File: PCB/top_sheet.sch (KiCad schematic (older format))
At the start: 0 parts

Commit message: PCB Edge.Cuts Defined
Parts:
- added FID1, FID2, FID3: Fiducial, local:Fiducial_Front_Layer, symbol Fiducial
- added PN1: PCB_LABEL, symbol PCB_LABEL
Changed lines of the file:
@@
 $Descr A 11000 8500
 encoding utf-8
-Sheet 2 5
-Title ""
-Date ""
-Rev ""
-Comp ""
+Sheet 2 20
+Title "Christmas Tree Disco"
+Date "2017-08-01"
+Rev "01"
+Comp "www.GitHub.com/Cryochasm"
 Comment1 ""
 Comment2 ""
@@
 F1 "rgb_led_array.sch" 60
 $EndSheet
+$Comp
+L PCB_LABEL PN1
+U 1 1 59822887
+P 5000 2100
+F 0 "PN1" H 5528 2246 50  0000 L CNN
+F 1 "PCB_LABEL" H 5528 2155 50  0000 L CNN
+F 2 "" H 5150 1900 60  0001 C CNN
+F 3 "" H 5150 1900 60  0001 C CNN
+	1    5000 2100
+	1    0    0    -1
+$EndComp
+$Comp
+L Fiducial FID3
+U 1 1 598229D8
+P 9200 1900
+F 0 "FID3" H 9306 1900 50  0000 L CNN
+F 1 "Fiducial" H 9200 1760 50  0001 C CNN
+F 2 "local:Fiducial_Front_Layer" H 9200 1900 60  0001 C CNN
+F 3 "" H 9200 1900 60  0001 C CNN
+	1    9200 1900
+	1    0    0    -1
+$EndComp
+$Comp
+L Fiducial FID2
+U 1 1 59822A8A
+P 9100 5700
+F 0 "FID2" H 9206 5700 50  0000 L CNN
+F 1 "Fiducial" H 9100 5560 50  0001 C CNN
+F 2 "local:Fiducial_Front_Layer" H 9100 5700 60  0001 C CNN
+F 3 "" H 9100 5700 60  0001 C CNN
+	1    9100 5700
+	1    0    0    -1
+$EndComp
+$Comp
+L Fiducial FID1
+U 1 1 59822B9A
+P 2600 5600
+F 0 "FID1" H 2706 5600 50  0000 L CNN
+F 1 "Fiducial" H 2600 5460 50  0001 C CNN
+F 2 "local:Fiducial_Front_Layer" H 2600 5600 60  0001 C CNN
+F 3 "" H 2600 5600 60  0001 C CNN
+	1    2600 5600
+	1    0    0    -1
+$EndComp
 $EndSCHEMATC

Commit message: Added Logic Level Conversion
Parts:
- removed FID1, FID2, FID3: Fiducial, local:Fiducial_Front_Layer, symbol Fiducial
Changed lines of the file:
@@
 $Descr A 11000 8500
 encoding utf-8
-Sheet 2 19
+Sheet 2 20
 Title "Christmas Tree Disco"
 Date "2017-08-01"
@@
 F0 "Microcontroller" 60
 F1 "microcontroller.sch" 60
+F2 "~~POWER[0..1]" I R 6000 4500 50
+F3 "~~SHIFT_CTRL[0..4]" B R 6000 5000 50
 $EndSheet
 $Sheet
@@
 F0 "RGB LED Array" 60
 F1 "rgb_led_array.sch" 60
+F2 "~~POWER[0..1]" I L 6600 4500 50
+F3 "~~SHIFT_CTRL[0..4]" B L 6600 5000 50
 $EndSheet
 $Comp
@@
 	1    0    0    -1
 $EndComp
-$Comp
-L Fiducial FID3
-U 1 1 598229D8
-P 9200 1900
-F 0 "FID3" H 9306 1900 50  0000 L CNN
-F 1 "Fiducial" H 9200 1760 50  0001 C CNN
-F 2 "local:Fiducial_Front_Layer" H 9200 1900 60  0001 C CNN
-F 3 "" H 9200 1900 60  0001 C CNN
-	1    9200 1900
-	1    0    0    -1
-$EndComp
-$Comp
-L Fiducial FID2
-U 1 1 59822A8A
-P 9100 5700
-F 0 "FID2" H 9206 5700 50  0000 L CNN
-F 1 "Fiducial" H 9100 5560 50  0001 C CNN
-F 2 "local:Fiducial_Front_Layer" H 9100 5700 60  0001 C CNN
-F 3 "" H 9100 5700 60  0001 C CNN
-	1    9100 5700
-	1    0    0    -1
-$EndComp
-$Comp
-L Fiducial FID1
-U 1 1 59822B9A
-P 2600 5600
-F 0 "FID1" H 2706 5600 50  0000 L CNN
-F 1 "Fiducial" H 2600 5460 50  0001 C CNN
-F 2 "local:Fiducial_Front_Layer" H 2600 5600 60  0001 C CNN
-F 3 "" H 2600 5600 60  0001 C CNN
-	1    2600 5600
-	1    0    0    -1
-$EndComp
+$Sheet
+S 1200 2600 1700 2600
+U 5984D7F4
+F0 "Power Supply" 50
+F1 "power.sch" 50
+$EndSheet
 $EndSCHEMATC

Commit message: Preliminary PCB layout
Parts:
- added H3: Snow Silk Screen, local:snow, symbol Generic
- V1.0: renamed from PN1; value PCB_LABEL -> www.github.com/Cryochasm; footprint (none) -> local:PCB-LABEL; Description (none) -> -; Included in BOM (none) -> No; MPN (none) -> -
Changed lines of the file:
@@
 F0 "Microcontroller" 60
 F1 "microcontroller.sch" 60
-F2 "~~POWER[0..1]" I R 6000 4500 50
+F2 "~~POWER[0..1]" I L 3500 2700 50
 F3 "~~SHIFT_CTRL[0..4]" B R 6000 5000 50
 $EndSheet
@@
 F0 "RGB LED Array" 60
 F1 "rgb_led_array.sch" 60
-F2 "~~POWER[0..1]" I L 6600 4500 50
+F2 "~~POWER[0..1]" I L 6600 2700 50
 F3 "~~SHIFT_CTRL[0..4]" B L 6600 5000 50
 $EndSheet
 $Comp
-L PCB_LABEL PN1
+L PCB_LABEL V1.0
 U 1 1 59822887
 P 5000 2100
-F 0 "PN1" H 5528 2246 50  0000 L CNN
-F 1 "PCB_LABEL" H 5528 2155 50  0000 L CNN
-F 2 "" H 5150 1900 60  0001 C CNN
-F 3 "" H 5150 1900 60  0001 C CNN
+F 0 "V1.0" H 4900 2200 50  0000 L CNN
+F 1 "www.github.com/Cryochasm" H 4500 2500 50  0000 L CNN
+F 2 "local:PCB-LABEL" H 5150 1900 60  0001 C CNN
+F 3 "-" H 5150 1900 60  0001 C CNN
+F 4 "-" H 5000 2100 60  0001 C CNN "MPN"
+F 5 "-" H 5000 2100 60  0001 C CNN "Description"
+F 6 "No" H 5000 2100 60  0001 C CNN "Included in BOM"
 	1    5000 2100
 	1    0    0    -1
@@
 F0 "Power Supply" 50
 F1 "power.sch" 50
+F2 "~~POWER[0..1]" I R 2900 2700 50
 $EndSheet
+Wire Bus Line
+	2900 2700 3500 2700
+Wire Bus Line
+	3400 2700 3400 2400
+Wire Bus Line
+	3400 2400 6100 2400
+Wire Bus Line
+	6100 2400 6100 2700
+Wire Bus Line
+	6100 2700 6600 2700
+Text Label 3600 2400 0    50   ~ 0
+~~POWER[0..1]
+Wire Bus Line
+	6000 5000 6600 5000
+$Comp
+L Generic H3
+U 1 1 5987C99A
+P 6100 2000
+F 0 "H3" H 6228 2046 50  0000 L CNN
+F 1 "Snow Silk Screen" H 6228 1955 50  0000 L CNN
+F 2 "local:snow" H 6100 1800 50  0001 C CNN
+F 3 "-" H 6100 2000 50  0001 C CNN
+F 4 "-" H 6100 1700 50  0001 C CNN "MPN"
+F 5 "-" H 6100 1600 50  0001 C CNN "Description"
+F 6 "No" H 6100 1500 50  0001 C CNN "Included in BOM"
+	1    6100 2000
+	1    0    0    -1
+$EndComp
+Text Label 2900 2700 0    50   ~ 0
+~~POWER[0..1]
 $EndSCHEMATC

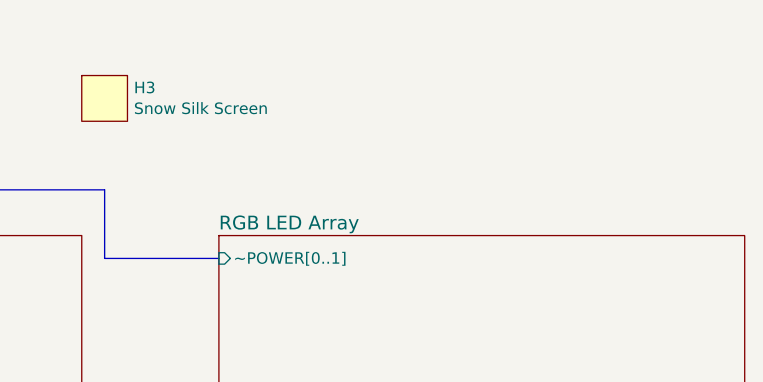
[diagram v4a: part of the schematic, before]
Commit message: V1.0 Ready for Review
Added compatability with the 430BOOST-C55AUDIO1 booster pack.
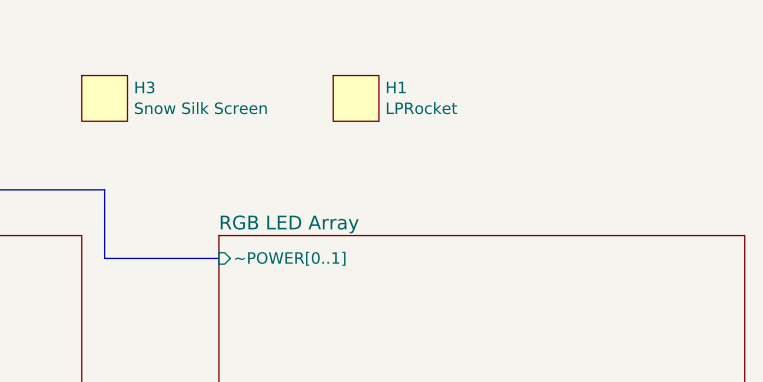
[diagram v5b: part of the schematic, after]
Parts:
- added H1: LPRocket, local:LPRocket, symbol Generic
- V1.0: footprint local:PCB-LABEL -> local:Cryochasm
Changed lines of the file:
@@
 Sheet 2 20
 Title "Christmas Tree Disco"
-Date "2017-08-01"
+Date "2017-08-08"
 Rev "01"
 Comp "www.GitHub.com/Cryochasm"
@@
 F 0 "V1.0" H 4900 2200 50  0000 L CNN
 F 1 "www.github.com/Cryochasm" H 4500 2500 50  0000 L CNN
-F 2 "local:PCB-LABEL" H 5150 1900 60  0001 C CNN
+F 2 "local:Cryochasm" H 5150 1900 60  0001 C CNN
 F 3 "-" H 5150 1900 60  0001 C CNN
 F 4 "-" H 5000 2100 60  0001 C CNN "MPN"
@@
 Text Label 2900 2700 0    50   ~ 0
 ~~POWER[0..1]
+$Comp
+L Generic H1
+U 1 1 598A6860
+P 7200 2000
+F 0 "H1" H 7328 2046 50  0000 L CNN
+F 1 "LPRocket" H 7328 1955 50  0000 L CNN
+F 2 "local:LPRocket" H 7200 1800 50  0001 C CNN
+F 3 "-" H 7200 2000 50  0001 C CNN
+F 4 "-" H 7200 1600 50  0001 C CNN "Description"
+F 5 "-" H 7200 1700 50  0001 C CNN "MPN"
+F 6 "No" H 7200 1500 50  0001 C CNN "Included in BOM"
+	1    7200 2000
+	1    0    0    -1
+$EndComp
 $EndSCHEMATC

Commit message: Gerber Updates
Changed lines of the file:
@@
 Title "Christmas Tree Disco"
 Date "2017-08-08"
-Rev "01"
+Rev "V1.0"
 Comp "www.GitHub.com/Cryochasm"
 Comment1 ""
@@
 U 1 1 59822887
 P 5000 2100
-F 0 "V1.0" H 4900 2200 50  0000 L CNN
+F 0 "V1.0" H 5200 2200 50  0000 L CNN
 F 1 "www.github.com/Cryochasm" H 4500 2500 50  0000 L CNN
 F 2 "local:Cryochasm" H 5150 1900 60  0001 C CNN

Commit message: Added Open Hardware Logo
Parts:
- added H7: SPFMDBC, local:Open_Source_HW_Logo, symbol Generic
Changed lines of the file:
@@
 Sheet 2 20
 Title "Christmas Tree Disco"
-Date "2017-08-08"
+Date "2017-08-15"
 Rev "V1.0"
 Comp "www.GitHub.com/Cryochasm"
@@
 	1    0    0    -1
 $EndComp
+$Comp
+L Generic H7
+U 1 1 59934D6E
+P 8000 2000
+F 0 "H7" H 8128 2046 50  0000 L CNN
+F 1 "SPFMDBC" H 8128 1955 50  0000 L CNN
+F 2 "local:Open_Source_HW_Logo" H 8000 1800 50  0001 C CNN
+F 3 "-" H 8000 2000 50  0001 C CNN
+F 4 "-" H 8000 1700 50  0001 C CNN "MPN"
+F 5 "-" H 8000 1600 50  0001 C CNN "Description"
+F 6 "No" H 8000 1500 50  0001 C CNN "Included in BOM"
+	1    8000 2000
+	1    0    0    -1
+$EndComp

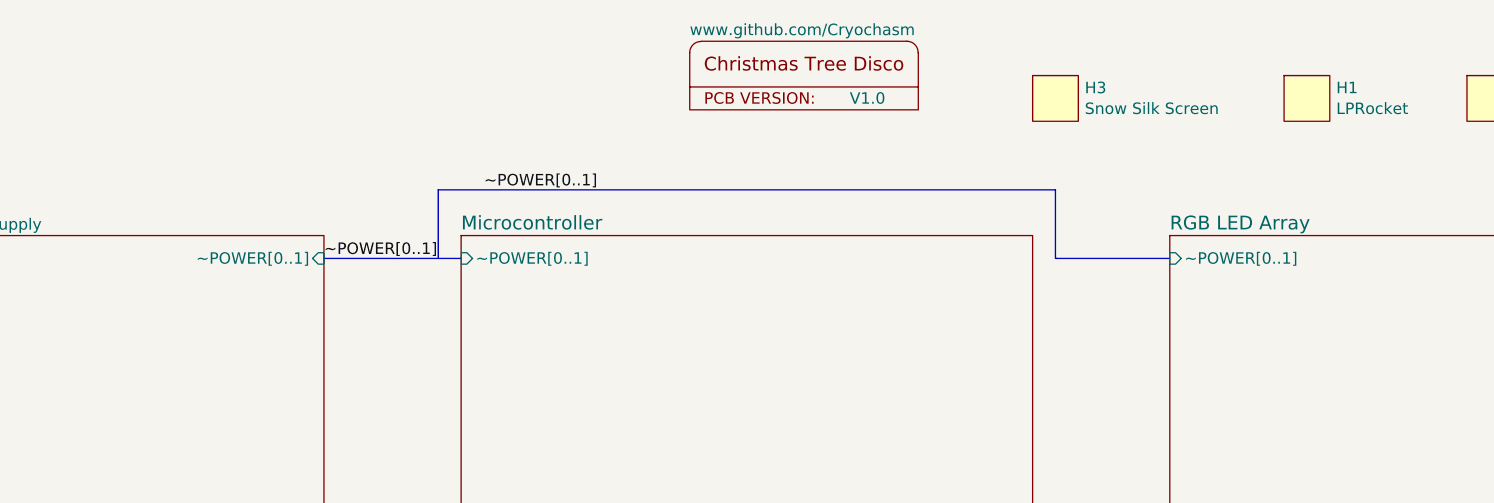
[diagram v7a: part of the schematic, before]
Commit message: Removed Level Shifter, Cleaned up gerbers
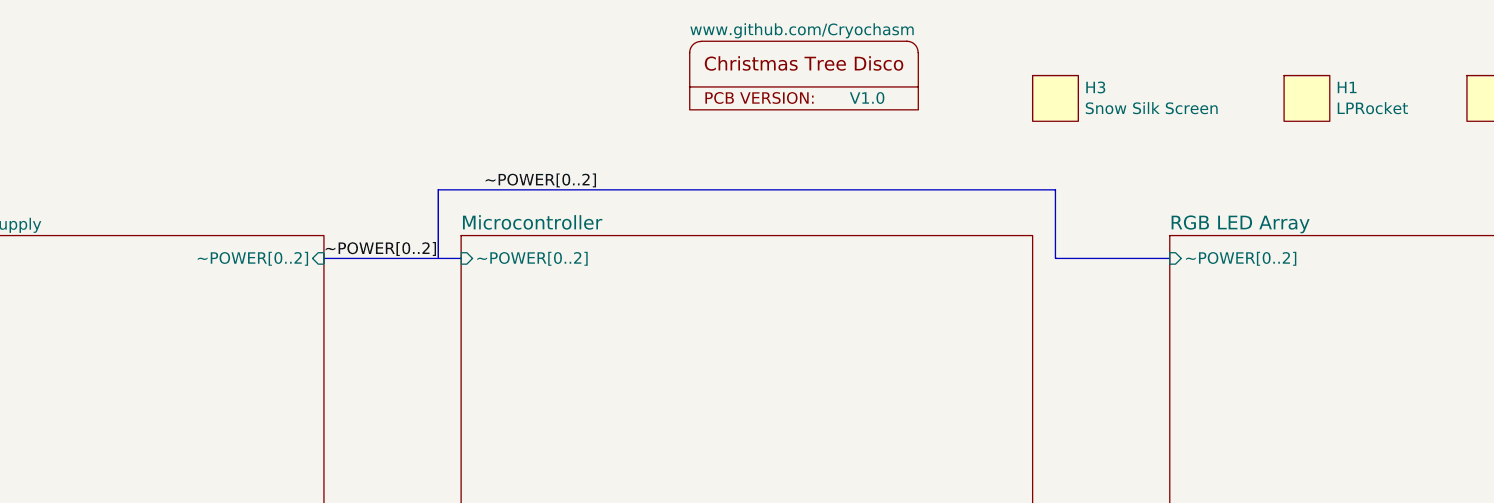
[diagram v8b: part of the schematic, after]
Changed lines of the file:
@@
 Sheet 2 20
 Title "Christmas Tree Disco"
-Date "2017-08-15"
+Date "2017-08-23"
 Rev "V1.0"
 Comp "www.GitHub.com/Cryochasm"
@@
 F0 "Microcontroller" 60
 F1 "microcontroller.sch" 60
-F2 "~~POWER[0..1]" I L 3500 2700 50
+F2 "~~POWER[0..2]" I L 3500 2700 50
 F3 "~~SHIFT_CTRL[0..4]" B R 6000 5000 50
 $EndSheet
@@
 F0 "RGB LED Array" 60
 F1 "rgb_led_array.sch" 60
-F2 "~~POWER[0..1]" I L 6600 2700 50
+F2 "~~POWER[0..2]" I L 6600 2700 50
 F3 "~~SHIFT_CTRL[0..4]" B L 6600 5000 50
 $EndSheet
@@
 F0 "Power Supply" 50
 F1 "power.sch" 50
-F2 "~~POWER[0..1]" I R 2900 2700 50
+F2 "~~POWER[0..2]" I R 2900 2700 50
 $EndSheet
 Wire Bus Line
@@
 	6100 2700 6600 2700
 Text Label 3600 2400 0    50   ~ 0
-~~POWER[0..1]
+~~POWER[0..2]
 Wire Bus Line
 	6000 5000 6600 5000
@@
 $EndComp
 Text Label 2900 2700 0    50   ~ 0
-~~POWER[0..1]
+~~POWER[0..2]
 $Comp
 L Generic H1
